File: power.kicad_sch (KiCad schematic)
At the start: 0 parts

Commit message: misc work, usb sch done
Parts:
- added C13, C14, C15: 2.2uF, Capacitor_SMD:C_0402_1005Metric, symbol Device:C
- added C16, C17, C18, C29, C30, C31, C32: 4.7uF, Capacitor_SMD:C_0402_1005Metric, symbol Device:C
- added C19, C20, C21, C22, C23, C24, C25, C26, C33: 10uF, symbol Device:C
- added C27, C28, C48, C49: 1uF, Capacitor_SMD:C_0402_1005Metric, symbol Device:C
- added C34, C35, C36, C37, C38, C39, C40, C41, C42, C43, C44, C46: 22uF, symbol Device:C
- added C45, C47: 18pF, Capacitor_SMD:C_0402_1005Metric, symbol Device:C
- added L1, L2, L3, L5, L6: 0.47uH, symbol Device:L
- added L4: 1uH, symbol Device:L
- added R10, R11: 100K, symbol Device:R
- added R9: 1M, symbol Device:R
- added TP10, TP11, TP12, TP13, TP14, TP15, TP16, TP17, TP18, TP19, TP20, TP4, TP5, TP6, TP7, TP8, TP9: TestPoint, TestPoint:TestPoint_Pad_D1.0mm, symbol Connector:TestPoint
- added U16: BD71847MWV, qsbc:UQFN56BV7070, symbol qsbc:BD71847MWV
- added Y1: Crystal, Crystal:Crystal_SMD_2012-2Pin_2.0x1.2mm, symbol Device:Crystal
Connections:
- new net: C47.1, R9.2, U16.13 (XOUT), Y1.2
- new net: C45.1, R9.1, U16.14 (XIN), Y1.1
- new net: R11.2, U16.40 (~{PWRON})
- new net BUCK1_LX: L1.1, U16.19 (BUCK1_LX), U16.20 (BUCK1_LX)
- new net BUCK2_LX: L2.1, U16.21 (BUCK2_LX), U16.22 (BUCK2_LX)
- new net BUCK5_LX: L3.1, U16.33 (BUCK5_LX), U16.34 (BUCK5_LX)
- new net BUCK6_LX: L4.1, U16.49 (BUCK6_LX), U16.50 (BUCK6_LX)
- new net BUCK7_LX: L5.1, U16.51 (BUCK7_LX), U16.52 (BUCK7_LX)
- new net BUCK8_LX: L6.1, U16.35 (BUCK8_LX), U16.36 (BUCK8_LX)
- new net CLK_32K_OUT: U16.29 (C33K_OUT)
- new net GND: C13.2, C14.2, C15.2, C16.2, C17.2, C18.2, C19.2, C20.2, C21.2, C22.2, C23.2, C24.2, C25.2, C26.2, C27.2, C28.2, C29.2, C30.2, C31.2, C32.2, C33.2, C34.2, C35.2, C36.2, C37.2, C38.2, C39.2, C40.2, C41.2, C42.2, C43.2, C44.2, C45.2, C46.2, C47.2, C48.2, C49.2, TP4.1, TP5.1, TP6.1, TP7.1, U16.12 (AGND), U16.57 (PGND), U16.58 (PGND), U16.59 (PGND), U16.60 (PGND), U16.61 (PGND)
- new net I2C1_SCL: U16.26 (SCL)
- new net I2C1_SDA: U16.27 (SDA)
- new net INTLDO_1.5V: C49.1, U16.11 (INTLDO1P5)
- new net LDO5_3.3V: C32.1, TP16.1, U16.4 (LDO5_VOUT)
- new net NVCC_DRAM_1.2V: C34.1, C35.1, L6.2, TP10.1, U16.38 (BUCK8_FB)
- new net NVCC_SD2: C33.1, TP17.1, U16.55 (MUXSW_VOUT)
- new net NVCC_SNVS_1P8: C27.1, C48.1, R11.1, TP11.1, U16.10 (LDO1_VOUT), U16.28 (DVDD)
- new net PMIC_ON_REQ: U16.15 (PMIC_ON_REQ)
- new net PMIC_STBY_REQ: U16.16 (PMIC_STBY_REQ)
- new net SD_VSELECT: U16.45 (SD_VSELECT)
- new net VDDA_1.8V: C31.1, TP15.1, U16.6 (LDO3_VOUT)
- new net VDD_1.8V: C16.1, C18.1, C36.1, C37.1, L5.2, R10.1, TP9.1, U16.43 (VIN_1P8_1), U16.54 (BUCK7_FB), U16.56 (VIN_1P8_2)
- new net VDD_3.3V: C17.1, C38.1, C39.1, L4.2, TP8.1, U16.1 (VIN_3P3), U16.46 (BUCK6_FB), U16.7 (VIN_3P3)
- new net VDD_ARM_0.9V: C42.1, C43.1, L2.2, TP19.1, U16.24 (BUCK2_FB)
- new net VDD_DRAM_xPU_0.9V: C40.1, C41.1, L3.2, TP20.1, U16.30 (BUCK5_FB)
- new net VDD_PHY_0.9V: C29.1, TP13.1, U16.42 (LDO4_VOUT)
- new net VDD_PHY_1.2V: C30.1, TP14.1, U16.44 (LDO6_VOUT)
- new net VDD_SNVS_0.8V: C28.1, TP12.1, U16.8 (LDO2_VOUT)
- new net VDD_SOC_0.8V: C44.1, C46.1, L1.2, TP18.1, U16.17 (BUCK1_FB)
- new net VSYS_5V: C13.1, C14.1, C15.1, C19.1, C20.1, C21.1, C22.1, C23.1, C24.1, C25.1, C26.1, U16.18 (BUCK1_VIN), U16.23 (BUCK2_VIN), U16.31 (BUCK5_VIN), U16.32 (BUCK5_VIN), U16.37 (BUCK8_VIN), U16.41 (VSYS), U16.47 (BUCK6_VIN), U16.48 (BUCK6_VIN), U16.5 (VSYS), U16.53 (BUCK7_VIN), U16.9 (VSYS)
- new net ~{PMIC_INT}: U16.39 (~{INT})
- new net ~{POR}: U16.25 (~{POR})
- new net ~{RTC_RESET}: U16.3 (~{RTC_RESET})
- new net ~{WDOG}: R10.2, U16.2 (~{WDOG})
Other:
- note added: "0.8V -> 0.85V 3A"
- note added: "0.8V 10mA"
- note added: "0.9V -> 0.85V/0.95V/1.0V 3A"
- note added: "0.9V -> 0.975V 3A"
- note added: "0.9V 250mA"
- note added: "1.1V -> 1.2V 3A"
- note added: "1.2V 300mA"
- note added: "1.8V 1.5A"
- note added: "1.8V 10mA"
- note added: "1.8V 300mA"
- note added: "3.3V 3A"
- note added: "3.3V/1.8V 150mA"

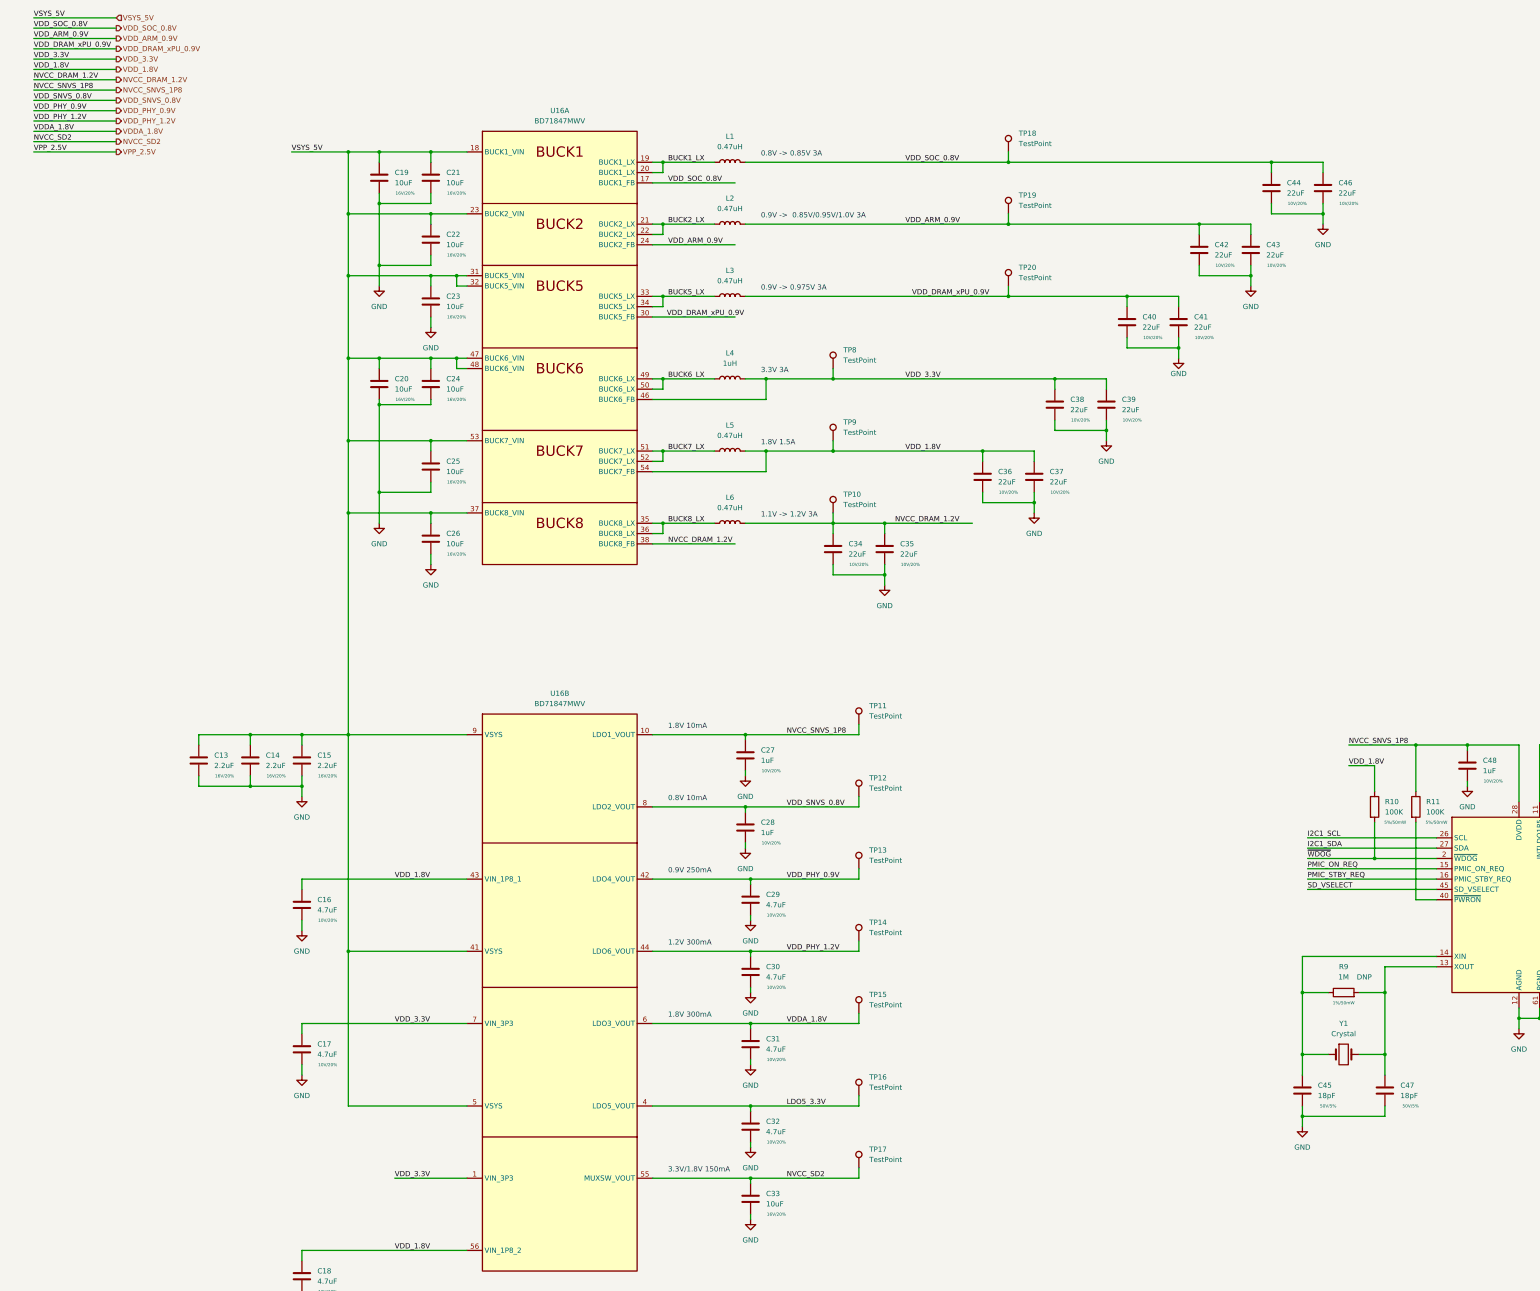
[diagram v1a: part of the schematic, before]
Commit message: ddr: add dual die support, misc work
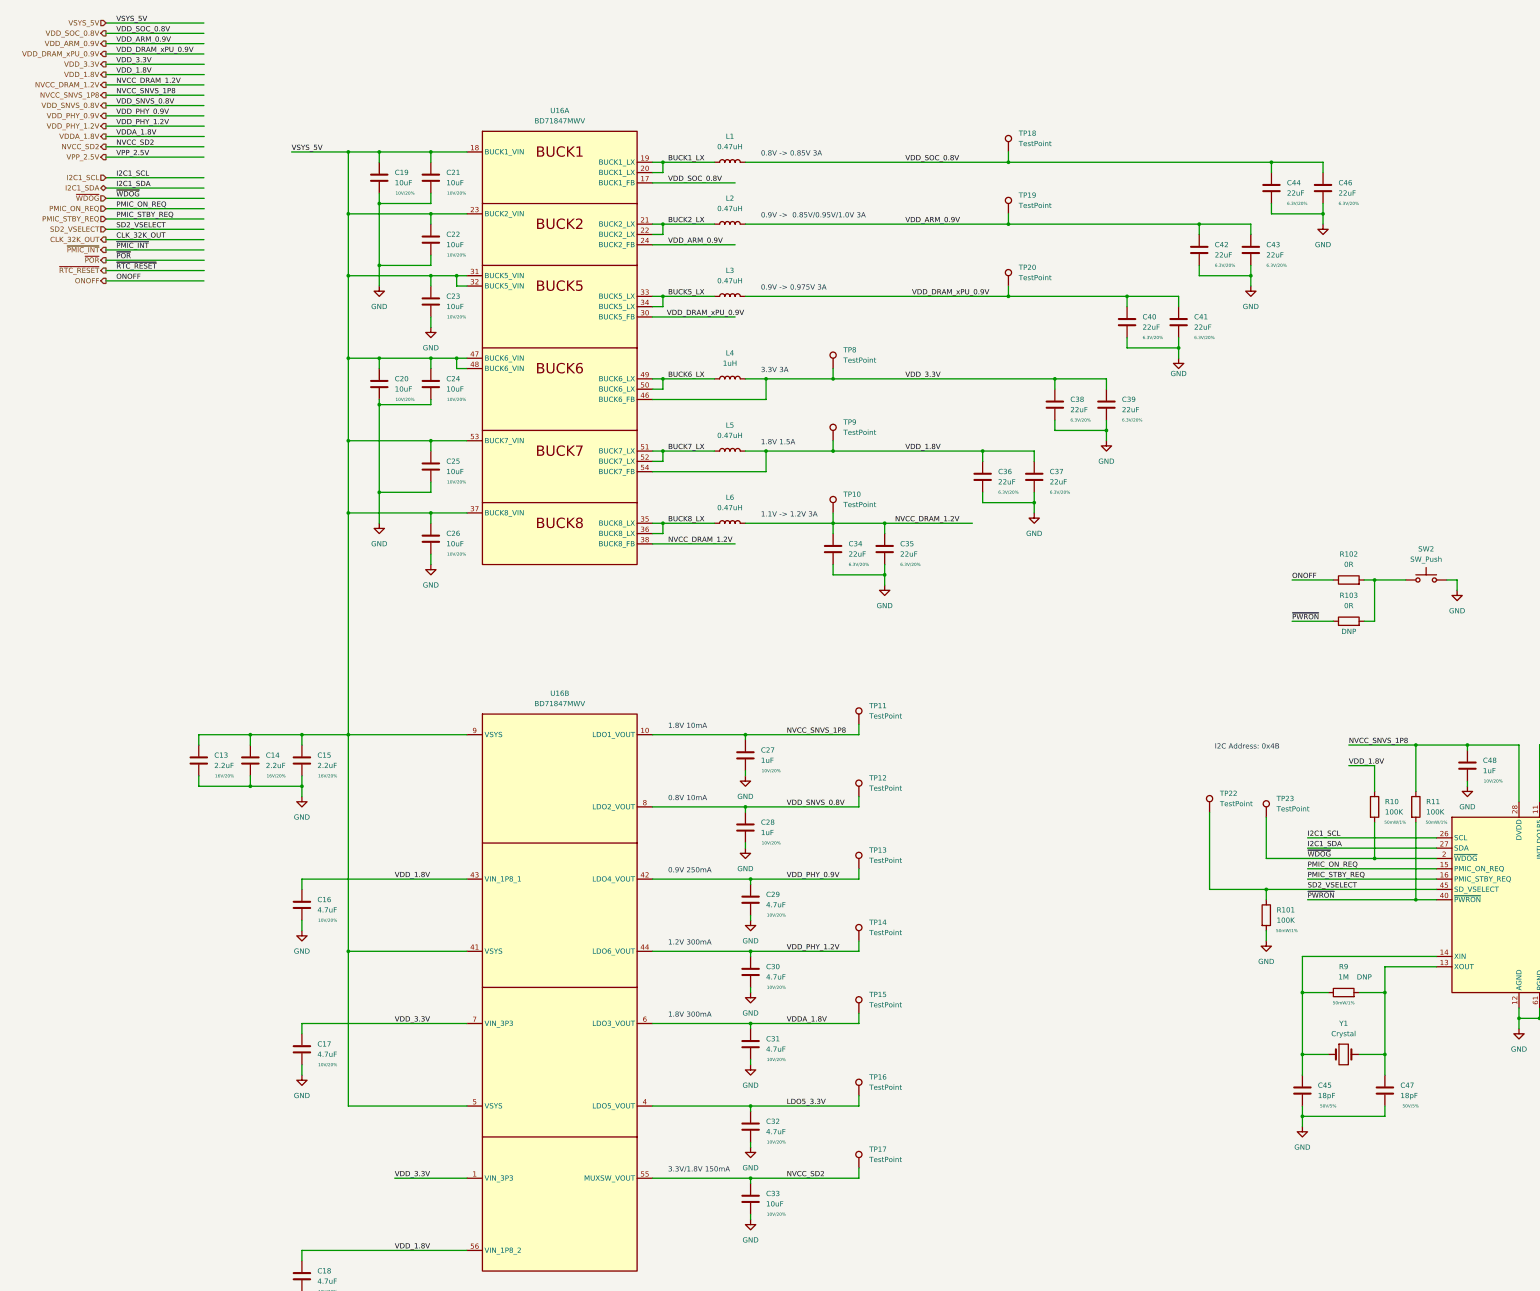
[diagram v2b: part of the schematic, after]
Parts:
- added R101: 100K, Resistor_SMD:R_0402_1005Metric, symbol Device:R
- added R102, R103: 0R, Resistor_SMD:R_0402_1005Metric, symbol Device:R
- added SW2: SW_Push, Button_Switch_THT:SW_Tactile_SPST_Angled_PTS645Vx58-2LFS, symbol Switch:SW_Push
- added TP22, TP23: TestPoint, TestPoint:TestPoint_Pad_D1.0mm, symbol Connector:TestPoint
- C19, C20, C21, C22, C23, C24, C25, C26, C33: footprint (none) -> Capacitor_SMD:C_0603_1608Metric; Rating 16V/20% -> 10V/20%
- C34, C35, C36, C37, C38, C39, C40, C41, C42, C43, C44, C46: footprint (none) -> Capacitor_SMD:C_0603_1608Metric; Rating 10V/20% -> 6.3V/20%
- L1, L2, L3, L4, L5, L6: footprint (none) -> Inductor_SMD:L_1008_2520Metric
- R10, R11: footprint (none) -> Resistor_SMD:R_0402_1005Metric; Rating 5%/50mW -> 50mW/1%
- R9: footprint (none) -> Resistor_SMD:R_0402_1005Metric; Rating 1%/50mW -> 50mW/1%
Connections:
- net GND: now also R101.2, SW2.2
- net ~{WDOG}: now also TP23.1
- net ~{PWRON}: now reaches R11.2, U16.40 (~{PWRON})
- net ~{PWRON}: now also R103.1
- net SD_VSELECT renamed SD2_VSELECT
- net SD2_VSELECT: now also R101.1, TP22.1
- new net: R102.2, R103.2, SW2.1
- new net ONOFF: R102.1
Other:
- note added: "I2C Address: 0x4B"
- company: (none) -> Q-LAB
- title: (none) -> QSBC

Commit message: fix ref desgigators, add table for dram config
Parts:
- renumbered C43 to C100, C44 to C101, C45 to C102, C46 to C103, C47 to C104, C48 to C105, C49 to C106, C13 to C70, C14 to C71, C15 to C72, C16 to C73, C17 to C74, C18 to C75, C19 to C76, C20 to C77, C21 to C78, C22 to C79, C23 to C80, C24 to C81, C25 to C82, C26 to C83, C27 to C84, C28 to C85, C29 to C86, C30 to C87, C31 to C88, C32 to C89, C33 to C90, C34 to C91, C35 to C92, C36 to C93, C37 to C94, C38 to C95, C39 to C96, C40 to C97, C41 to C98, C42 to C99, R101 to R13, R9 to R14, R102 to R15, R103 to R16, R10 to R17, R11 to R18, SW2 to SW1, TP22 to TP21, TP23 to TP22, U16 to U3
